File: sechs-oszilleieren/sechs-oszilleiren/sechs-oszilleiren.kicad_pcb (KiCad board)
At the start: 2 copper layers, 41.7 x 112 mm, 82 parts, among them J101 AudioJack2, J102 AudioJack2, J103 AudioJack2, J104 AudioJack2, J105 AudioJack2, J106 AudioJack2, J107 AudioJack2, J108 AudioJack2, J109 AudioJack2, J110 Conn_IDC_Box_Header_02x05_Top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, J111 AudioJack2, J112 AudioJack2, Q101 2N3904, Q102 2N3904, Q103 2N3904, Q104 2N3904, Q105 2N3904, Q106 2N3904, Q107 2N3904, U101 40106, U102 TL072

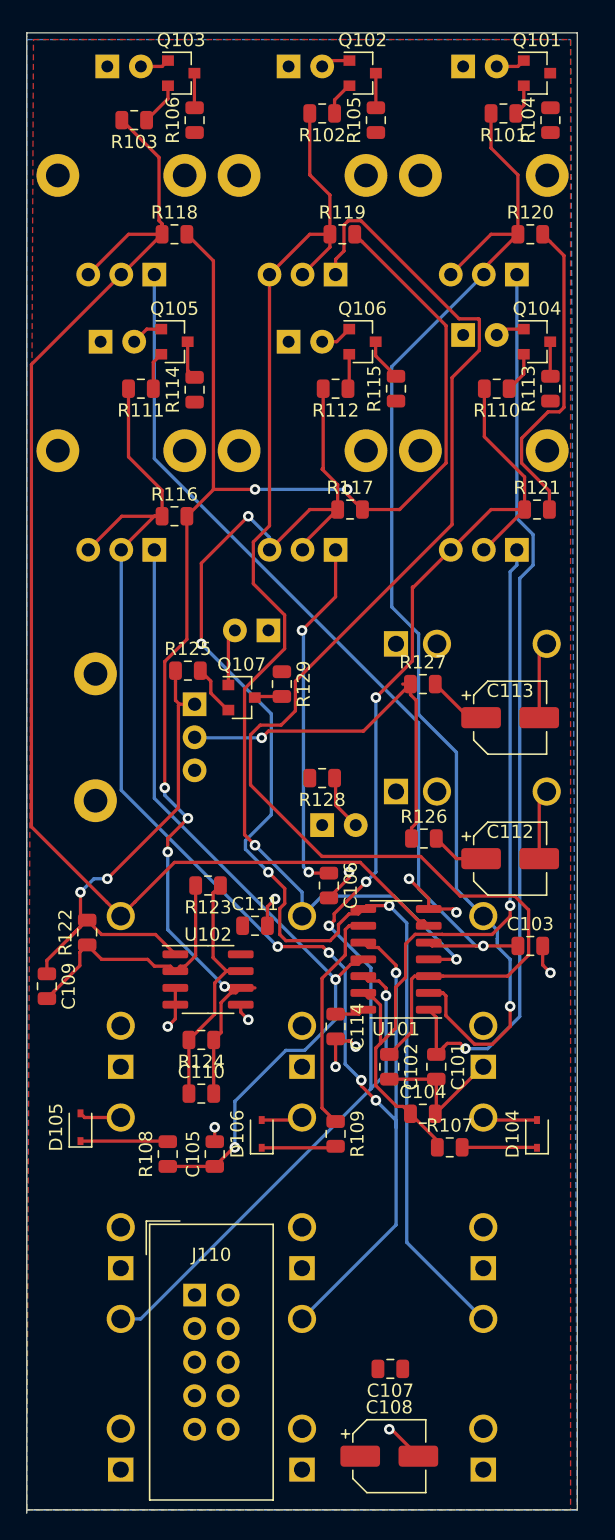
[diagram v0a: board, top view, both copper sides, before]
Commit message: Totally rerouted the board to make sure all connections are made. It's still an awful mess, so I think board layout needs to be carefully reconsidered if I want to fit it  in this form factor...
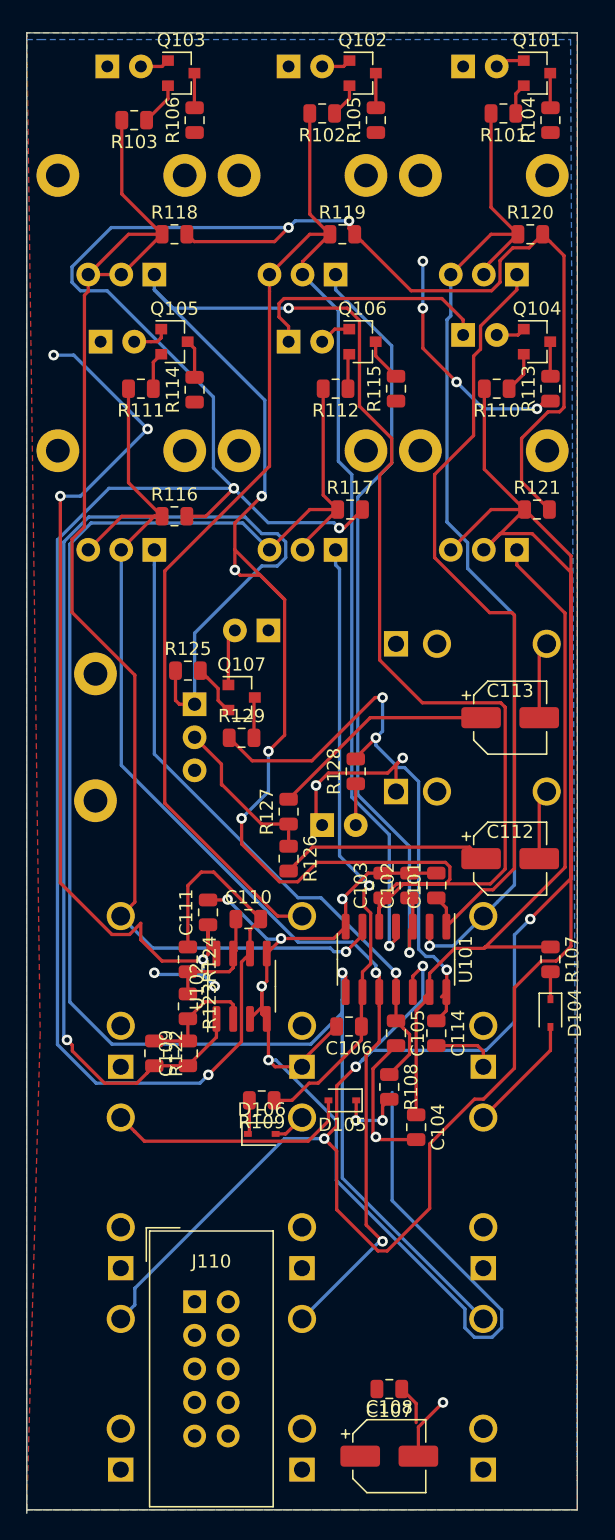
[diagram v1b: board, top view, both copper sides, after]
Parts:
- moved D105 19.9 mm to (105.2, 100.1), turned to 180 degrees
- moved R108 17.5 mm to (108.7, 99.1), turned to 270 degrees
- moved C105 16.5 mm to (109.2, 95.0), turned to 270 degrees
- moved R107 16.1 mm to (120.9, 89.4), turned to 270 degrees
- moved R127 14.0 mm to (101.1, 78.2), turned to 90 degrees
- moved C102 13.8 mm to (110.2, 83.8), turned to 90 degrees
- moved C101 13.7 mm to (112.3, 83.8), turned to 90 degrees
- moved C110 13.7 mm to (98.0, 86.4)
- moved C103 12.1 mm to (108.2, 83.8), turned to 90 degrees
- moved C109 11.8 mm to (93.5, 96.5), turned to 90 degrees
- moved C106 10.8 mm to (105.7, 94.5), turned to 180 degrees
- moved R122 10.5 mm to (90.9, 96.5), turned to 270 degrees
- moved R126 10.4 mm to (101.1, 81.8), turned to 270 degrees
- moved R123 9.27 mm to (93.5, 93.0), turned to 270 degrees
- moved D104 9.20 mm to (120.9, 93.5), turned to 270 degrees
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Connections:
- J110 pad 1: (no net) -> +12V
- J110 pad 2: (no net) -> +12V
- J110 pad 3: (no net) -> GND
- J110 pad 4: (no net) -> GND
- J110 pad 5: (no net) -> GND
- J110 pad 6: (no net) -> GND
- J110 pad 7: (no net) -> GND
- J110 pad 8: (no net) -> GND
- R128 pad 2: Net-(J110-Pad+12) -> +12V
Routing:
- net +12V: track 2.23 -> 136.3 mm, vias 0 -> 13
- net GND: track 36.2 -> 149.5 mm, vias 11 -> 9
- net Net-(C103-Pad1): track 68.3 -> 162.2 mm, vias 1 -> 5
- net /MIX_F: track 103.9 -> 193.9 mm
- net Net-(C110-Pad2): track 138.2 -> 205.4 mm, vias 6 -> 5
- net Net-(C109-Pad1): track 38.8 -> 91.5 mm, vias 2 -> 1
- net Net-(C102-Pad1): track 105.2 -> 60.1 mm, vias 0 -> 1
- net /MIX_B: track 89.0 -> 132.0 mm, vias 2 -> 1
- net /MIX_D: track 105.1 -> 127.5 mm, vias 4 -> 1
- net Net-(R126-Pad1): track 30.6 -> 12.4 mm, vias 1 -> 0
- net /MIX_A: track 94.8 -> 79.6 mm
- net Net-(D105-Pad2): track 3.54 -> 18.6 mm
- net /MIX_E: track 108.7 -> 93.8 mm, vias 5 -> 2
- net Net-(C105-Pad1): track 63.3 -> 49.4 mm, vias 2 -> 1
- net Net-(C113-Pad1): track 4.52 -> 17.1 mm
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
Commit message: I don't remember how this changed, but git tells me it did...
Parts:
- moved C105 40.8 mm to (93.5, 57.4), turned to 90 degrees
- moved R122 28.9 mm to (100.1, 69.1), turned to 180 degrees
- moved R123 26.2 mm to (104.1, 69.1), turned to 180 degrees
- moved R116 26.0 mm to (98.0, 81.3), turned to 90 degrees
- moved C109 25.8 mm to (100.1, 71.6), turned to 0 degrees
- moved R107 23.1 mm to (113.3, 111.3)
- moved D105 22.0 mm to (83.3, 102.6), turned to 90 degrees
- moved D111 20.2 mm to (84.3, 77.7), turned to 90 degrees
- moved R108 19.1 mm to (89.9, 102.6)
- moved C111 16.9 mm to (104.1, 71.6), turned to 0 degrees
- moved R126 16.1 mm to (104.6, 66.0)
- moved R129 15.7 mm to (83.8, 65.0)
- moved R128 15.6 mm to (90.9, 71.6)
- moved U102 15.5 mm to (100.1, 76.2), turned to 0 degrees
- moved U101 15.3 mm to (110.2, 104.6), turned to 180 degrees
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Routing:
- net +12V: track 136.3 -> 1.88 mm, vias 13 -> 0
- net Net-(C110-Pad2): track 205.4 -> 95.8 mm, vias 5 -> 2
- net GND: track 149.5 -> 51.4 mm, vias 9 -> 6
- net /MIX_F: track 193.9 -> 113.5 mm, vias 4 -> 2
- net Net-(C103-Pad1): track 162.2 -> 92.4 mm, vias 5 -> 4
- net Net-(C109-Pad1): track 91.5 -> 26.7 mm, vias 1 -> 3
- net /MIX_D: track 127.5 -> 82.0 mm, vias 1 -> 2
- net Net-(C101-Pad1): track 60.5 -> 88.8 mm, vias 0 -> 2
- net /MIX_B: track 132.0 -> 105.8 mm, vias 1 -> 2
- net Net-(C105-Pad1): track 49.4 -> 73.3 mm
- net Net-(C102-Pad1): track 60.1 -> 83.0 mm, vias 1 -> 6
- net /MIX_A: track 79.6 -> 100.2 mm, vias 1 -> 2
- net Net-(D105-Pad2): track 18.6 -> 3.63 mm
- net /MIX_C: track 96.6 -> 110.9 mm, vias 1 -> 0
- net Net-(C104-Pad1): track 55.3 -> 69.6 mm, vias 0 -> 2
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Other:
- net class Power added: clearance 0.4, trace_width 0.4, via_dia 0.8, via_drill 0.4
- net class Signal added: clearance 0.4, trace_width 0.25, via_dia 0.6, via_drill 0.3

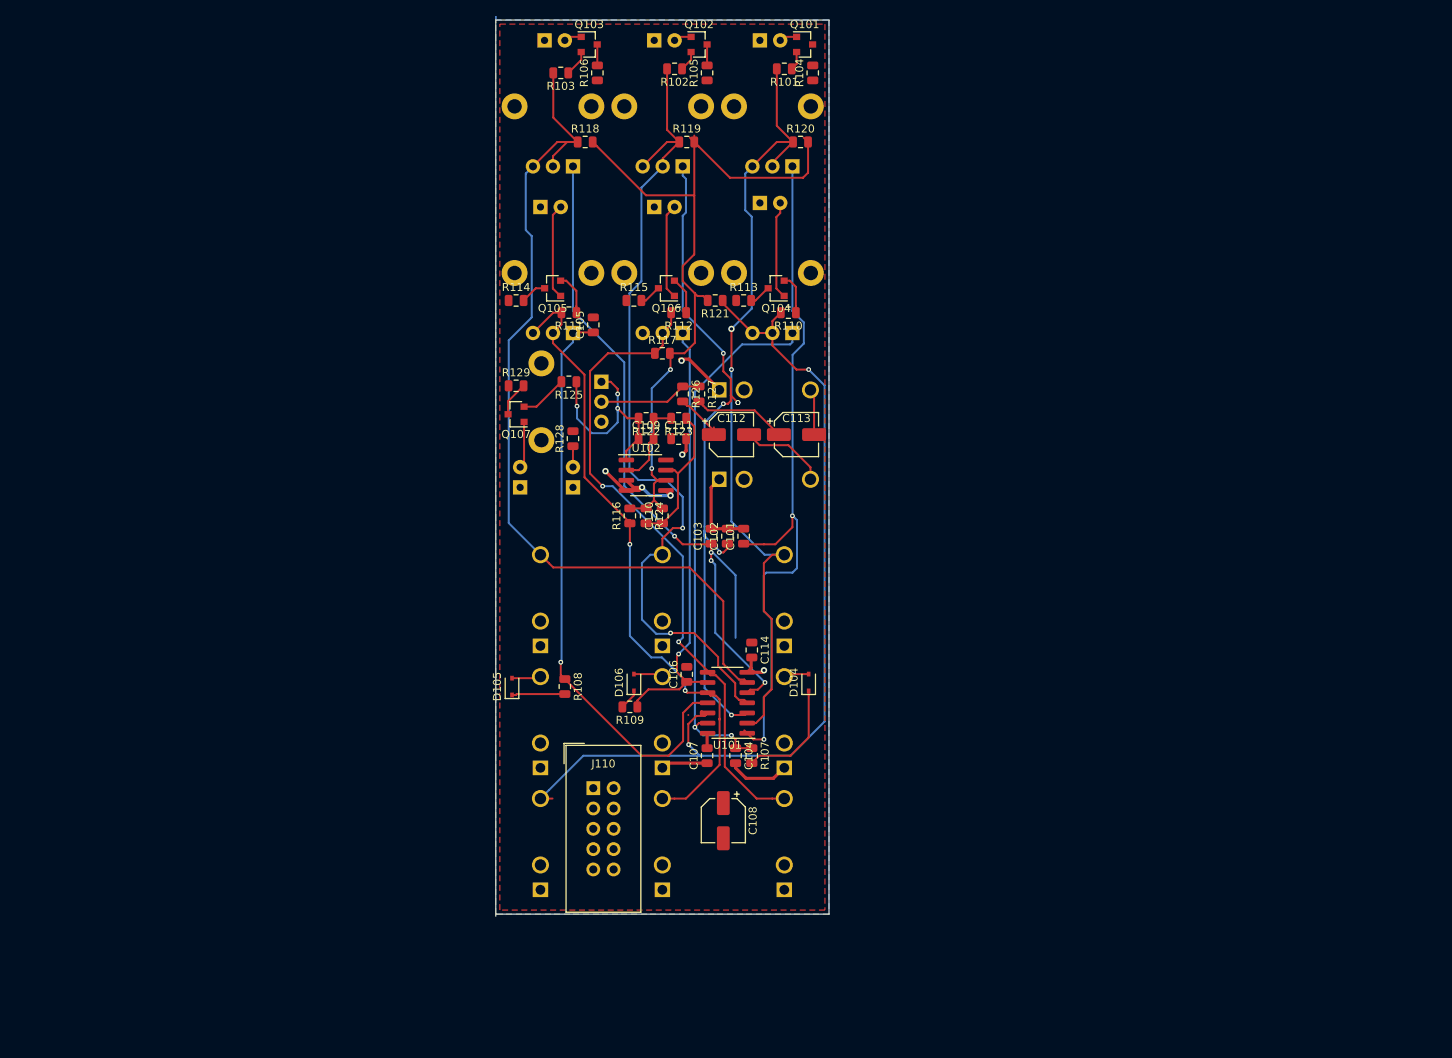
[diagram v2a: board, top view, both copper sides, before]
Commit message: Started rearranging the components on the boards such that a panel may also be laid out in FR4
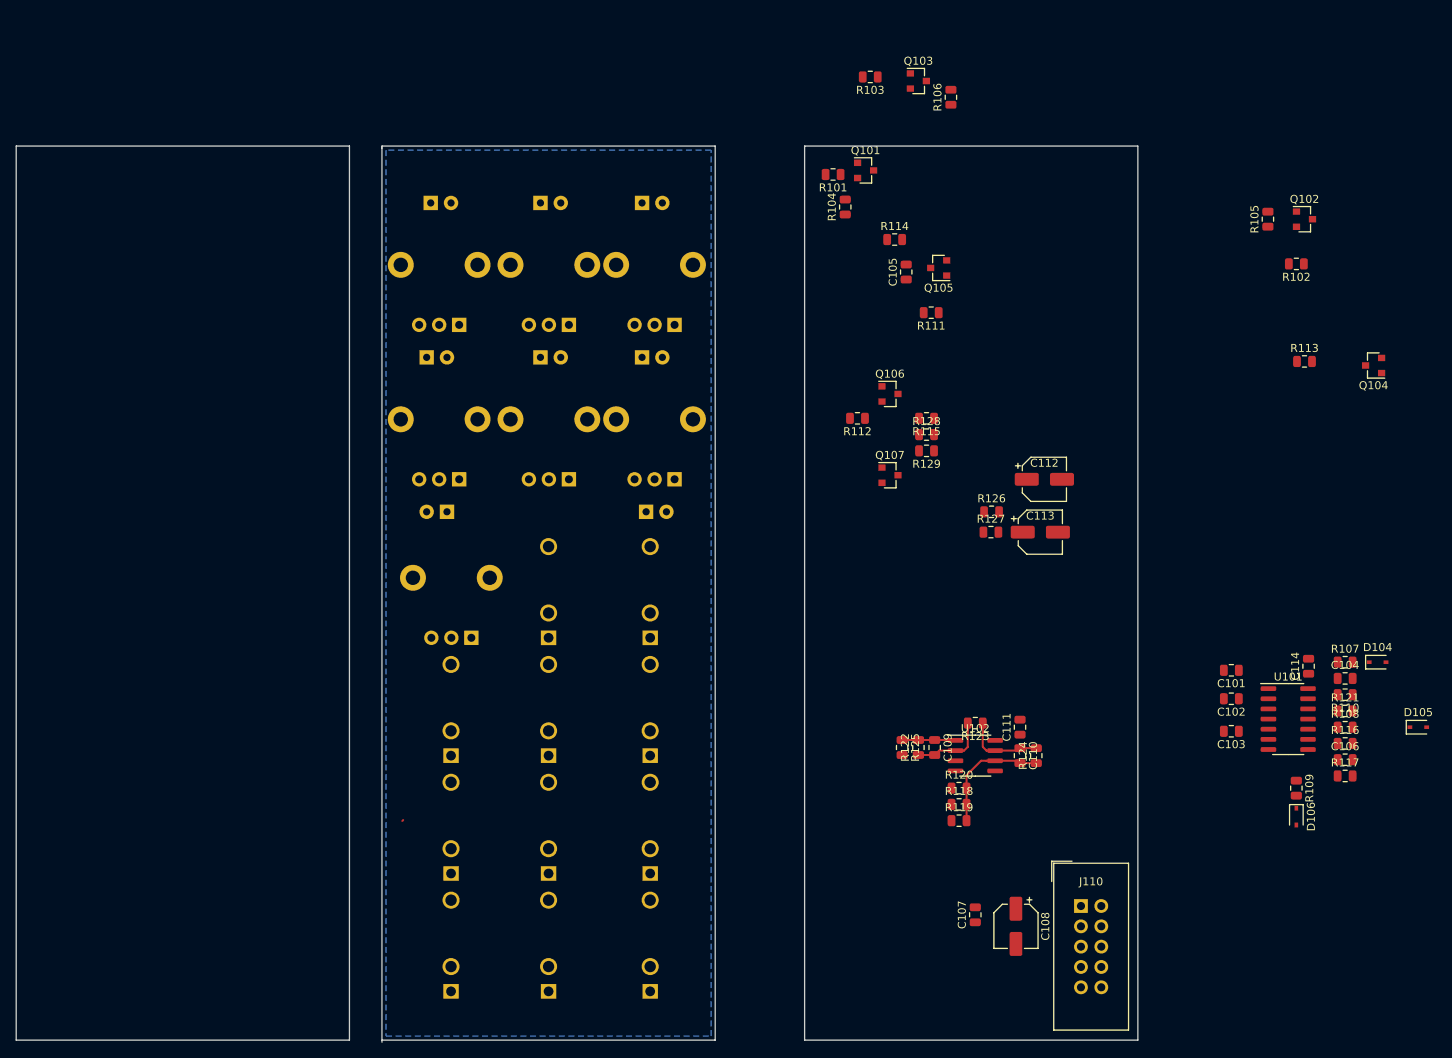
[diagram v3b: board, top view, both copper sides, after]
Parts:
- moved D105 113.4 mm to (196.6, 107.7), turned to 0 degrees
- moved R117 100.4 mm to (187.5, 113.8)
- moved R108 97.7 mm to (187.5, 107.7), turned to 0 degrees
- moved R118 95.1 mm to (139.2, 117.3)
- moved R121 94.0 mm to (187.5, 105.7), turned to 0 degrees
- moved R116 93.8 mm to (187.5, 109.7), turned to 0 degrees
- moved R119 91.4 mm to (139.2, 119.4)
- moved D106 84.5 mm to (181.4, 118.9), turned to 270 degrees
- moved R110 84.4 mm to (187.5, 103.6)
- moved R109 83.9 mm to (181.4, 115.3), turned to 270 degrees
- moved R120 83.2 mm to (139.2, 115.3)
- moved C106 83.0 mm to (187.5, 111.8), turned to 0 degrees
- moved R102 81.5 mm to (181.4, 49.8)
- moved Q102 78.8 mm to (182.4, 44.2)
- moved C104 76.8 mm to (187.5, 101.6), turned to 0 degrees
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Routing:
- net /MIX_F: track 113.5 -> 0.00 mm, vias 2 -> 0
- net /MIX_C: track 110.9 -> 0.00 mm
- net /MIX_B: track 105.8 -> 0.00 mm, vias 2 -> 0
- net /MIX_A: track 100.2 -> 0.00 mm, vias 2 -> 0
- net Net-(C103-Pad1): track 92.4 -> 0.00 mm, vias 4 -> 0
- net Net-(C101-Pad1): track 88.8 -> 0.00 mm, vias 2 -> 0
- net Net-(C102-Pad1): track 83.0 -> 0.00 mm, vias 6 -> 0
- net /MIX_D: track 82.0 -> 0.00 mm, vias 2 -> 0
- net /MIX_E: track 82.0 -> 0.00 mm, vias 2 -> 0
- net Net-(C110-Pad2): track 95.8 -> 15.3 mm, vias 2 -> 0
- net Net-(C105-Pad1): track 73.3 -> 0.00 mm, vias 1 -> 0
- net Net-(C104-Pad1): track 69.6 -> 0.00 mm, vias 2 -> 0
- net Net-(C106-Pad1): track 55.7 -> 0.00 mm, vias 1 -> 0
- net GND: track 51.4 -> 0.00 mm, vias 6 -> 0
- net Net-(C109-Pad1): track 26.7 -> 6.69 mm, vias 3 -> 0
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- removed copper zone on F.Cu, net +12V
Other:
- board size 41.7 x 112 mm -> 140.2 x 112 mm

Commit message: Added pins between boards for stacking. Changed all components to THT components.
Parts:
- removed C101, C102, C103: 1.0uF, Capacitor_SMD:C_0805_2012Metric
- removed C104, C105, C106, C111, C114: 0.1uF, Capacitor_SMD:C_0805_2012Metric
- removed C107: 0.01uF, Capacitor_SMD:C_0805_2012Metric
- removed C108, C112, C113: 10uF, Capacitor_SMD:CP_Elec_5x5.4
- removed C109: 47pF, Capacitor_SMD:C_0805_2012Metric
- removed C110: 27pF, Capacitor_SMD:C_0805_2012Metric
- removed D101, D102, D103, D107, D108, D109, D110: R, LED_THT:LED_D3.0mm
- removed D104, D105, D106: 1N4148, Diode_SMD:D_SOD-323
- removed D111: Y, LED_THT:LED_D3.0mm
- removed J101, J102, J103, J104, J105, J106, J107, J108, J109, J111, J112: AudioJack2, Connector_Audio:Jack_3.5mm_QingPu_WQP-PJ398SM_Vertical_CircularHoles
- removed J110: Conn_IDC_Box_Header_02x05_Top_Bottom, Connectors_IDC:IDC-Header_2x05_Pitch2.54mm_Straight
- removed Q101, Q102, Q103, Q104, Q105, Q106, Q107: 2N3904, Package_TO_SOT_SMD:SOT-23
- removed R101, R102, R103, R110, R111, R112, R125: 47K, Resistor_SMD:R_0805_2012Metric
- removed R104, R105, R106, R113, R114, R115, R129: 2K, Resistor_SMD:R_0805_2012Metric
- removed R107, R108, R109: 1K, Resistor_SMD:R_0805_2012Metric
- removed R116, R117, R118, R119, R120, R121, R122, R123, R124: 10K, Resistor_SMD:R_0805_2012Metric
- removed R126, R127: 100R, Resistor_SMD:R_0805_2012Metric
- removed R128: 22K, Resistor_SMD:R_0805_2012Metric
- removed RV101, RV102, RV103, RV104, RV105, RV106: B100K, Potentiometer_THT:Potentiometer_Alpha_RD901F-40-00D_Single_Vertical_CircularHoles
- removed RV107: A10K, Potentiometer_THT:Potentiometer_Alpha_RD901F-40-00D_Single_Vertical_CircularHoles
- removed U101: 40106, Package_SO:SOIC-14_3.9x8.7mm_P1.27mm
- removed U102: TL072, Package_SO:SOIC-8_3.9x4.9mm_P1.27mm
- added C1: 1.0uF, Capacitor_THT:C_Rect_L7.2mm_W3.5mm_P5.00mm_FKS2_FKP2_MKS2_MKP2, F.Cu at (244.5, 226.7)
- added C10: 47pF, Capacitor_THT:C_Rect_L7.2mm_W2.5mm_P5.00mm_FKS2_FKP2_MKS2_MKP2, F.Cu at (231.0, 210.6)
- added C11: 27pF, Capacitor_THT:C_Disc_D4.7mm_W2.5mm_P5.00mm, F.Cu at (253.0, 226.2)
- added C12: 10uF, Capacitor_THT:CP_Radial_D5.0mm_P2.50mm, F.Cu at (253.5, 231.5)
- added C13: 10uF, Capacitor_THT:CP_Radial_D5.0mm_P2.50mm, F.Cu at (262.2, 221.3)
- added C14: 0.01uF, Capacitor_THT:C_Rect_L7.2mm_W2.5mm_P5.00mm_FKS2_FKP2_MKS2_MKP2, F.Cu at (211.3, 204.0)
- added C15: 10uF, Capacitor_THT:CP_Radial_D5.0mm_P2.50mm, F.Cu at (265.7, 199.3)
- added C2: 1.0uF, Capacitor_THT:C_Rect_L7.2mm_W3.5mm_P5.00mm_FKS2_FKP2_MKS2_MKP2, F.Cu at (253.3, 221.7)
- added C3: 1.0uF, Capacitor_THT:C_Rect_L7.2mm_W3.5mm_P5.00mm_FKS2_FKP2_MKS2_MKP2, F.Cu at (244.5, 221.7)
- added C4: 0.1uF, Capacitor_THT:C_Rect_L7.2mm_W2.5mm_P5.00mm_FKS2_FKP2_MKS2_MKP2, F.Cu at (253.3, 217.1)
- added C5: 0.1uF, Capacitor_THT:C_Rect_L7.2mm_W2.5mm_P5.00mm_FKS2_FKP2_MKS2_MKP2, F.Cu at (235.2, 231.9)
- added C6: 0.1uF, Capacitor_THT:C_Rect_L7.2mm_W2.5mm_P5.00mm_FKS2_FKP2_MKS2_MKP2, F.Cu at (244.5, 217.1)
- added C7: 0.1uF, Capacitor_THT:C_Rect_L7.2mm_W2.5mm_P5.00mm_FKS2_FKP2_MKS2_MKP2, F.Cu at (87.4, 189.0)
- added C8: 0.1uF, Capacitor_THT:C_Rect_L7.2mm_W2.5mm_P5.00mm_FKS2_FKP2_MKS2_MKP2, F.Cu at (226.4, 229.0)
- added C9: 0.1uF, Capacitor_THT:C_Rect_L7.2mm_W2.5mm_P5.00mm_FKS2_FKP2_MKS2_MKP2, F.Cu at (215.6, 232.5)
- added D1: R, LED_THT:LED_D3.0mm, F.Cu at (298.5, 150.6)
- added D10: 1N4148, Diode_THT:D_DO-35_SOD27_P7.62mm_Horizontal, F.Cu at (219.9, 210.3)
- added D11: 1N4148, Diode_THT:D_DO-35_SOD27_P7.62mm_Horizontal, F.Cu at (215.3, 228.7)
- added D2: R, LED_THT:LED_D3.0mm, F.Cu at (304.4, 145.1)
- added D3: R, LED_THT:LED_D3.0mm, F.Cu at (290.2, 159.2)
- added D4: R, LED_THT:LED_D3.0mm, F.Cu at (283.7, 165.3)
- added D5: R, LED_THT:LED_D3.0mm, F.Cu at (305.0, 139.3)
- added D6: R, LED_THT:LED_D3.0mm, F.Cu at (298.5, 145.1)
- added D7: R, LED_THT:LED_D3.0mm, F.Cu at (274.5, 169.1)
- added D8: Y, LED_THT:LED_D3.0mm, F.Cu at (290.2, 153.7)
- added D9: 1N4148, Diode_THT:D_DO-35_SOD27_P7.62mm_Horizontal, F.Cu at (200.3, 203.8)
- added J1: AudioJack2, Connector_Audio:Jack_3.5mm_QingPu_WQP-PJ398SM_Vertical_CircularHoles, F.Cu at (248.2, 115.2)
- added J10: AudioJack2, Connector_Audio:Jack_3.5mm_QingPu_WQP-PJ398SM_Vertical_CircularHoles, F.Cu at (228.6, 150.3)
- added J11: AudioJack2, Connector_Audio:Jack_3.5mm_QingPu_WQP-PJ398SM_Vertical_CircularHoles, F.Cu at (272.5, 108.6)
- added J12: AudioJack2, Connector_Audio:Jack_3.5mm_QingPu_WQP-PJ398SM_Vertical_CircularHoles, F.Cu at (259.3, 115.2)
- added J13: AudioJack2, Connector_Audio:Jack_3.5mm_QingPu_WQP-PJ398SM_Vertical_CircularHoles, F.Cu at (250.7, 130.6)
- added J14: AudioJack2, Connector_Audio:Jack_3.5mm_QingPu_WQP-PJ398SM_Vertical_CircularHoles, F.Cu at (239.6, 150.3)
- added J15: AudioJack2, Connector_Audio:Jack_3.5mm_QingPu_WQP-PJ398SM_Vertical_CircularHoles, F.Cu at (-42.3, 33.1)
- added J16: Conn_01x02_Male, Connector_PinHeader_2.54mm:PinHeader_1x02_P2.54mm_Vertical, F.Cu at (220.7, 152.6)
- added J17: AudioJack2, Connector_Audio:Jack_3.5mm_QingPu_WQP-PJ398SM_Vertical_CircularHoles, F.Cu at (228.6, 134.8)
- added J18: AudioJack2, Connector_Audio:Jack_3.5mm_QingPu_WQP-PJ398SM_Vertical_CircularHoles, F.Cu at (239.6, 134.8)
- added J19: Conn_01x09_Male, Connector_PinHeader_2.54mm:PinHeader_1x09_P2.54mm_Vertical, B.Cu at (60.5, 88.4)
- added J2: AudioJack2, Connector_Audio:Jack_3.5mm_QingPu_WQP-PJ398SM_Vertical_CircularHoles, F.Cu at (-20.2, 33.1)
- added J20: Conn_01x12_Male, Connector_PinHeader_2.54mm:PinHeader_1x12_P2.54mm_Vertical, B.Cu at (24.4, 88.4)
- added J21: Conn_01x06_Male, Connector_PinHeader_2.54mm:PinHeader_1x06_P2.54mm_Vertical, F.Cu at (220.7, 135.2)
- added J22: Conn_01x05_Male, Connector_PinHeader_2.54mm:PinHeader_1x05_P2.54mm_Vertical, F.Cu at (264.0, 161.9)
- added J23: Conn_IDC_Box_Header_02x05_Top_Bottom, Connectors_IDC:IDC-Header_2x05_Pitch2.54mm_Straight, F.Cu at (102.6, 140.2)
- added J24: Conn_01x02_Female, Connector_PinSocket_2.54mm:PinSocket_1x02_P2.54mm_Vertical, F.Cu at (265.9, 191.2)
- added J25: Conn_01x09_Female, Connector_PinSocket_2.54mm:PinSocket_1x09_P2.54mm_Vertical, B.Cu at (105.7, 88.9)
- added J26: Conn_01x12_Female, Connector_PinSocket_2.54mm:PinSocket_1x12_P2.54mm_Vertical, B.Cu at (70.1, 88.4)
- added J27: Conn_01x06_Female, Connector_PinSocket_2.54mm:PinSocket_1x06_P2.54mm_Vertical, B.Cu at (70.1, 59.4)
- added J28: Conn_01x05_Female, Connector_PinSocket_2.54mm:PinSocket_1x05_P2.54mm_Vertical, F.Cu at (240.4, 217.4)
- added J3: AudioJack2, Connector_Audio:Jack_3.5mm_QingPu_WQP-PJ398SM_Vertical_CircularHoles, F.Cu at (261.7, 146.1)
- added J4: AudioJack2, Connector_Audio:Jack_3.5mm_QingPu_WQP-PJ398SM_Vertical_CircularHoles, F.Cu at (272.8, 124.1)
- added J5: AudioJack2, Connector_Audio:Jack_3.5mm_QingPu_WQP-PJ398SM_Vertical_CircularHoles, F.Cu at (294.6, 108.6)
- added J6: AudioJack2, Connector_Audio:Jack_3.5mm_QingPu_WQP-PJ398SM_Vertical_CircularHoles, F.Cu at (250.7, 146.1)
- added J7: AudioJack2, Connector_Audio:Jack_3.5mm_QingPu_WQP-PJ398SM_Vertical_CircularHoles, F.Cu at (-31.3, 33.1)
- added J8: AudioJack2, Connector_Audio:Jack_3.5mm_QingPu_WQP-PJ398SM_Vertical_CircularHoles, F.Cu at (283.5, 108.6)
- added J9: AudioJack2, Connector_Audio:Jack_3.5mm_QingPu_WQP-PJ398SM_Vertical_CircularHoles, F.Cu at (261.7, 130.6)
- added Q1: 2N3904, Package_TO_SOT_THT:TO-92, F.Cu at (268.3, 175.4)
- added Q2: 2N3904, Package_TO_SOT_THT:TO-92, F.Cu at (284.0, 160.0)
- added Q3: 2N3904, Package_TO_SOT_THT:TO-92, F.Cu at (309.9, 130.1)
- added Q4: 2N3904, Package_TO_SOT_THT:TO-92, F.Cu at (268.3, 169.6)
- added Q5: 2N3904, Package_TO_SOT_THT:TO-92, F.Cu at (298.8, 139.8)
- added Q6: 2N3904, Package_TO_SOT_THT:TO-92, F.Cu at (284.0, 154.2)
- added Q7: 2N3904, Package_TO_SOT_THT:TO-92, F.Cu at (309.9, 124.3)
- added R1: 47K, Resistor_THT:R_Axial_DIN0204_L3.6mm_D1.6mm_P7.62mm_Horizontal, F.Cu at (125.5, 74.2)
- added R10: 2K, Resistor_THT:R_Axial_DIN0204_L3.6mm_D1.6mm_P7.62mm_Horizontal, F.Cu at (125.5, 53.3)
- added R11: 2K, Resistor_THT:R_Axial_DIN0204_L3.6mm_D1.6mm_P7.62mm_Horizontal, F.Cu at (125.5, 68.1)
- added R12: 2K, Resistor_THT:R_Axial_DIN0204_L3.6mm_D1.6mm_P7.62mm_Horizontal, F.Cu at (125.5, 66.0)
- added R13: 22K, Resistor_THT:R_Axial_DIN0204_L3.6mm_D1.6mm_P7.62mm_Horizontal, F.Cu at (125.4, 55.4)
- added R14: 47K, Resistor_THT:R_Axial_DIN0204_L3.6mm_D1.6mm_P7.62mm_Horizontal, F.Cu at (125.5, 64.0)
- added R15: 2K, Resistor_THT:R_Axial_DIN0204_L3.6mm_D1.6mm_P7.62mm_Horizontal, F.Cu at (125.5, 62.0)
- added R16: 1K, Resistor_THT:R_Axial_DIN0204_L3.6mm_D1.6mm_P7.62mm_Horizontal, F.Cu at (200.7, 185.6)
- added R17: 1K, Resistor_THT:R_Axial_DIN0204_L3.6mm_D1.6mm_P7.62mm_Horizontal, F.Cu at (112.8, 161.5)
- added R18: 1K, Resistor_THT:R_Axial_DIN0204_L3.6mm_D1.6mm_P7.62mm_Horizontal, F.Cu at (200.7, 192.2)
- added R19: 10K, Resistor_THT:R_Axial_DIN0204_L3.6mm_D1.6mm_P7.62mm_Horizontal, F.Cu at (97.0, 168.1)
- added R2: 47K, Resistor_THT:R_Axial_DIN0204_L3.6mm_D1.6mm_P7.62mm_Horizontal, F.Cu at (138.2, 39.1)
- added R20: 10K, Resistor_THT:R_Axial_DIN0204_L3.6mm_D1.6mm_P7.62mm_Horizontal, F.Cu at (200.7, 198.7)
- added R21: 10K, Resistor_THT:R_Axial_DIN0204_L3.6mm_D1.6mm_P7.62mm_Horizontal, F.Cu at (224.9, 185.6)
- added R22: 10K, Resistor_THT:R_Axial_DIN0204_L3.6mm_D1.6mm_P7.62mm_Horizontal, F.Cu at (197.1, 210.3)
- added R23: 10K, Resistor_THT:R_Axial_DIN0204_L3.6mm_D1.6mm_P7.62mm_Horizontal, F.Cu at (224.9, 192.2)
- added R24: 10K, Resistor_THT:R_Axial_DIN0204_L3.6mm_D1.6mm_P7.62mm_Horizontal, F.Cu at (224.9, 198.7)
- added R25: 10K, Resistor_THT:R_Axial_DIN0204_L3.6mm_D1.6mm_P7.62mm_Horizontal, F.Cu at (74.7, 169.2)
- added R26: 10K, Resistor_THT:R_Axial_DIN0204_L3.6mm_D1.6mm_P7.62mm_Horizontal, F.Cu at (220.3, 205.3)
- added R27: 10K, Resistor_THT:R_Axial_DIN0204_L3.6mm_D1.6mm_P7.62mm_Horizontal, F.Cu at (104.6, 170.2)
- added R28: 47K, Resistor_THT:R_Axial_DIN0204_L3.6mm_D1.6mm_P7.62mm_Horizontal, F.Cu at (82.3, 166.6)
- added R29: 100R, Resistor_THT:R_Axial_DIN0204_L3.6mm_D1.6mm_P7.62mm_Horizontal, F.Cu at (249.2, 185.6)
- added R3: 47K, Resistor_THT:R_Axial_DIN0204_L3.6mm_D1.6mm_P7.62mm_Horizontal, F.Cu at (244.7, 110.0)
- added R30: 100R, Resistor_THT:R_Axial_DIN0204_L3.6mm_D1.6mm_P7.62mm_Horizontal, F.Cu at (240.0, 211.8)
- added R4: 2K, Resistor_THT:R_Axial_DIN0204_L3.6mm_D1.6mm_P7.62mm_Horizontal, F.Cu at (125.4, 76.2)
- added R5: 2K, Resistor_THT:R_Axial_DIN0204_L3.6mm_D1.6mm_P7.62mm_Horizontal, F.Cu at (125.5, 72.1)
- added R6: 2K, Resistor_THT:R_Axial_DIN0204_L3.6mm_D1.6mm_P7.62mm_Horizontal, F.Cu at (125.4, 59.5)
- added R7: 47K, Resistor_THT:R_Axial_DIN0204_L3.6mm_D1.6mm_P7.62mm_Horizontal, F.Cu at (125.5, 70.1)
- added R8: 47K, Resistor_THT:R_Axial_DIN0204_L3.6mm_D1.6mm_P7.62mm_Horizontal, F.Cu at (125.4, 57.5)
- added R9: 47K, Resistor_THT:R_Axial_DIN0204_L3.6mm_D1.6mm_P7.62mm_Horizontal, F.Cu at (125.5, 78.2)
- added RV1: B100K, Potentiometer_THT:Potentiometer_Alpha_RD901F-40-00D_Single_Vertical_CircularHoles, F.Cu at (280.0, 126.8)
- added RV2: B100K, Potentiometer_THT:Potentiometer_Alpha_RD901F-40-00D_Single_Vertical_CircularHoles, F.Cu at (301.8, 111.4)
- added RV3: B100K, Potentiometer_THT:Potentiometer_Alpha_RD901F-40-00D_Single_Vertical_CircularHoles, F.Cu at (248.6, 164.3)
- added RV4: B100K, Potentiometer_THT:Potentiometer_Alpha_RD901F-40-00D_Single_Vertical_CircularHoles, F.Cu at (268.9, 142.3)
- added RV5: B100K, Potentiometer_THT:Potentiometer_Alpha_RD901F-40-00D_Single_Vertical_CircularHoles, F.Cu at (294.8, 126.8)
- added RV6: B100K, Potentiometer_THT:Potentiometer_Alpha_RD901F-40-00D_Single_Vertical_CircularHoles, F.Cu at (283.7, 141.2)
- added RV7: A10K, Potentiometer_THT:Potentiometer_Alpha_RD901F-40-00D_Single_Vertical_CircularHoles, F.Cu at (268.9, 156.7)
- added U1: 40106, Package_DIP:DIP-14_W7.62mm_Socket_LongPads, F.Cu at (96.5, 62.0)
- added U2: TL072, Package_DIP:DIP-8_W7.62mm_Socket_LongPads, F.Cu at (85.9, 172.2)
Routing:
- net Net-(C110-Pad2): track 15.3 -> 0.00 mm
- net Net-(C110-Pad1): track 9.97 -> 0.00 mm
- net Net-(C109-Pad2): track 9.56 -> 0.00 mm
- net Net-(C109-Pad1): track 6.69 -> 0.00 mm
